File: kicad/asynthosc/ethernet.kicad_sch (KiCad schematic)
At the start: 40 parts, among them J12 RJ45_LED_Shielded, U10 LAN8742A, U11 USBLC6-2P6, U13 USBLC6-2P6, Y2 25MHZ,20PF,30PPM

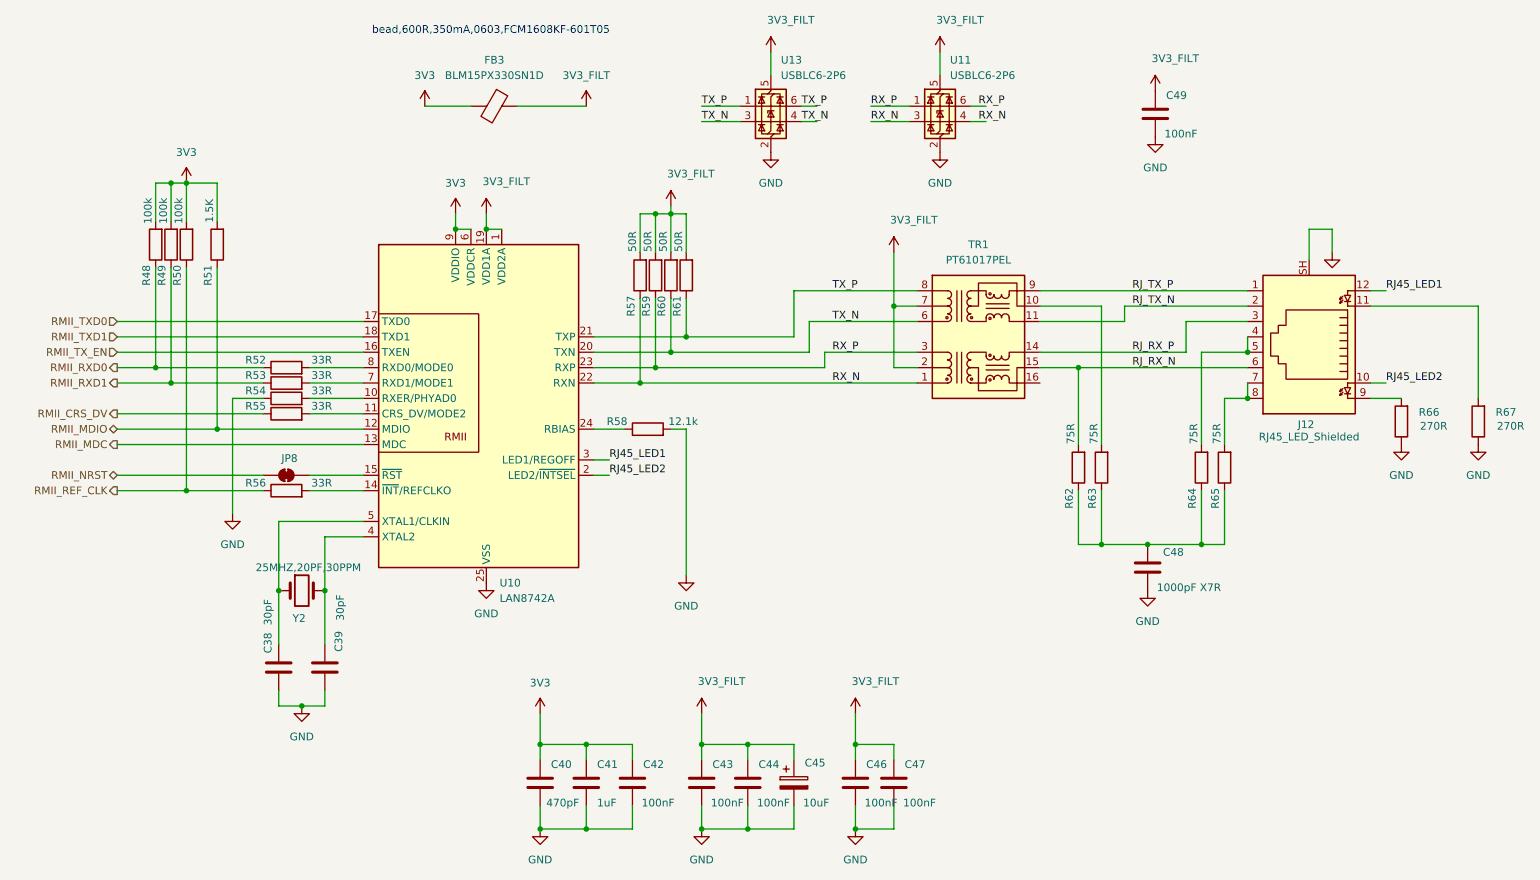
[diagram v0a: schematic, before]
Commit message: sch: pcb: fix pin errors
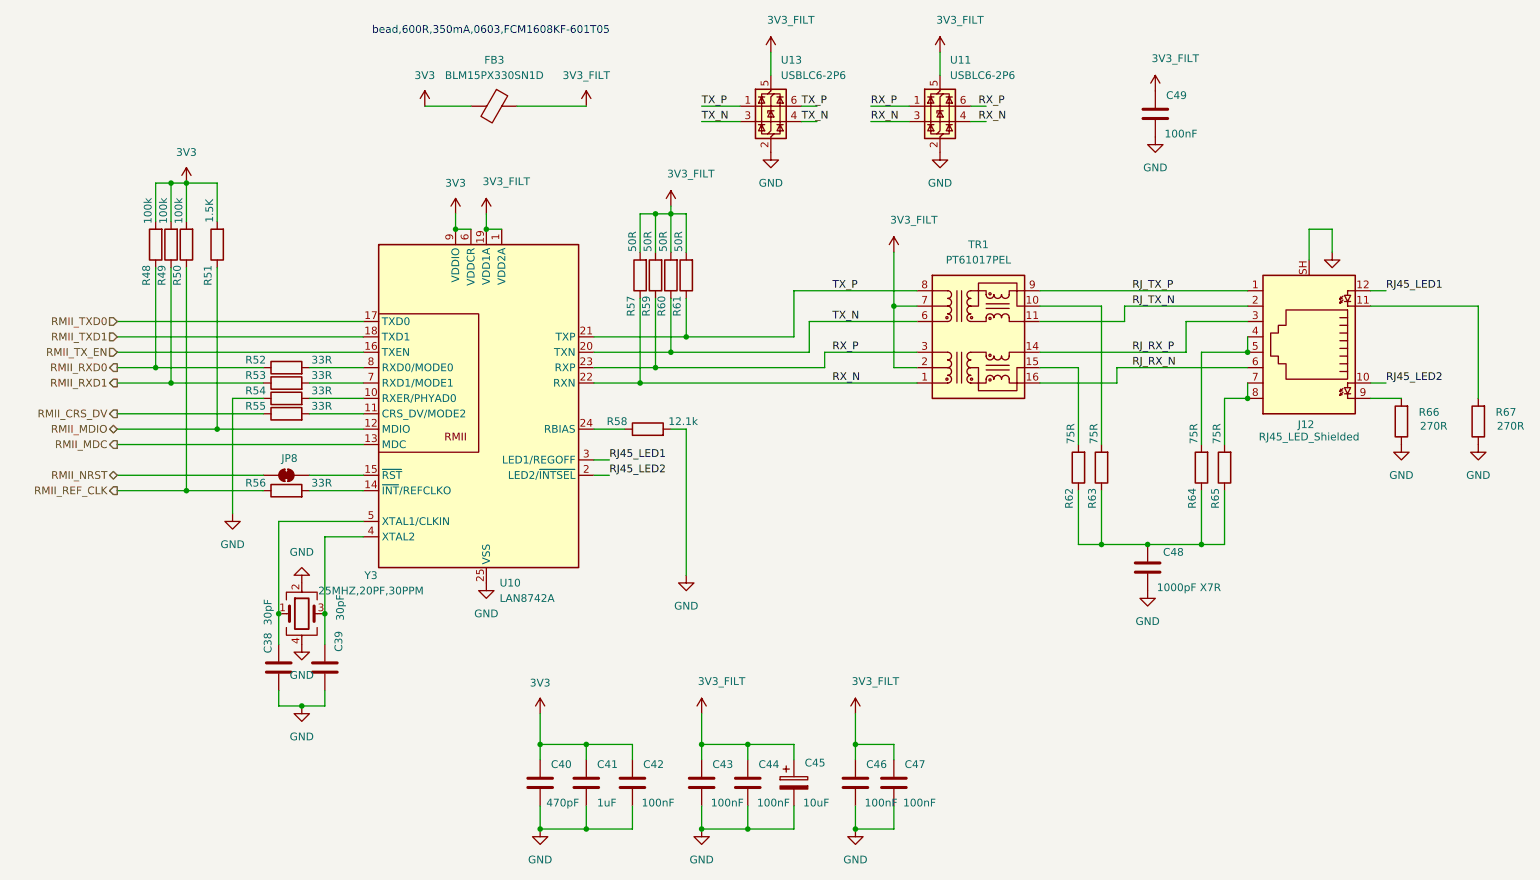
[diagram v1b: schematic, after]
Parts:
- removed Y2: 25MHZ,20PF,30PPM, Crystal:Crystal_SMD_3225-4Pin_3.2x2.5mm, symbol Device:Crystal
- added Y3: 25MHZ,20PF,30PPM, Crystal:Crystal_SMD_3225-4Pin_3.2x2.5mm, symbol Device:Crystal_GND24
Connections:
- net GND: now also Y3.2, Y3.4
- net RJ_RX_N: now also TR1.16 (TX+); no longer R62.2, TR1.15 (C_TX)
- net at C38.2, U10.5 (XTAL1/CLKIN): now also Y3.1
- net at C39.2, U10.4 (XTAL2): now also Y3.3
- new net: R62.2, TR1.15 (C_TX)

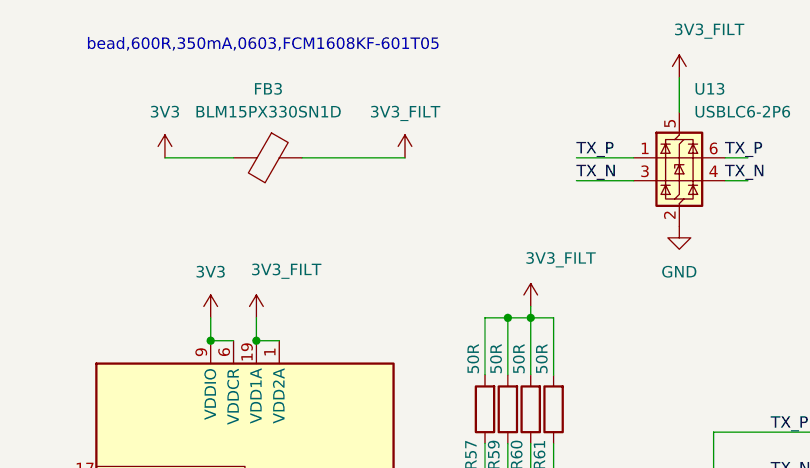
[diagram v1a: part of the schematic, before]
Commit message: pcb: route, add some silkscreen
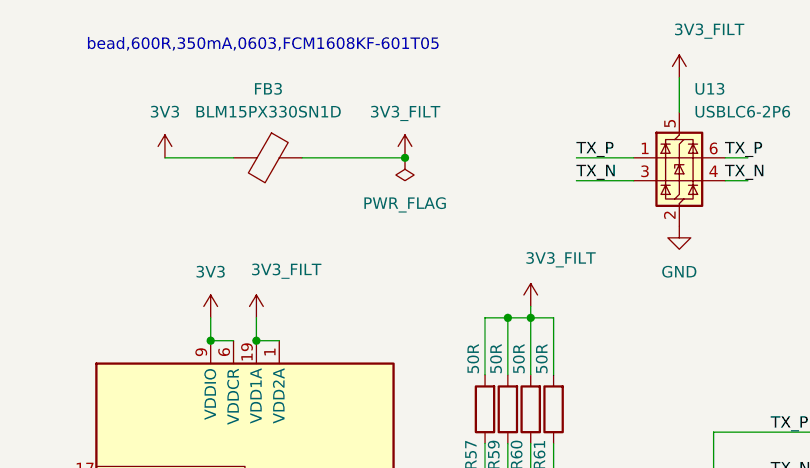
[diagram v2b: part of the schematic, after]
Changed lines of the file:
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@@
 	)
 	(junction
+		(at 106.68 31.75)
+		(diameter 0)
+		(color 0 0 0 0)
+	)
+	(junction
 		(at 118.11 74.93)
 		(diameter 0)
@@
 					(unit 1)
 				)
+			)
+		)
+	)
+	(symbol
+		(lib_id "power:PWR_FLAG")
+		(at 106.68 31.75 180)
+		(unit 1)
+		(exclude_from_sim no)
+		(in_bom yes)
+		(on_board yes)
+		(dnp no)
+		(fields_autoplaced yes)
+		(property "Reference" "#FLG06"
+			(at 106.68 33.655 0)
+			(effects
+				(font
+					(size 1.27 1.27)
+				)
+				(hide yes)
+			)
+		)
+		(property "Value" "PWR_FLAG"
+			(at 106.68 36.83 0)
+			(effects
+				(font
+					(size 1.27 1.27)
+				)
+			)
+		)
+		(property "Footprint" ""
+			(at 106.68 31.75 0)
+			(effects
+				(font
+					(size 1.27 1.27)
+				)
+				(hide yes)
+			)
+		)
+		(property "Datasheet" "~"
+			(at 106.68 31.75 0)
+			(effects
+				(font
+					(size 1.27 1.27)
+				)
+				(hide yes)
+			)
+		)
+		(property "Description" "Special symbol for telling ERC where power comes from"
+			(at 106.68 31.75 0)
+			(effects
+				(font
+					(size 1.27 1.27)
+				)
+				(hide yes)
+			)
+		)
+		(pin "1"
+		)
+		(instances
+			(project "asynthosc"
+				(path "/d73e377a-a016-415f-8824-91cc6e4907b9/dee5e89d-6774-4f8d-b6d8-6a859b9e32e8/354f1097-74a0-4bc1-8721-d2c0e4c9dab3"
+					(reference "#FLG06")
+					(unit 1)
+				)

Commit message: comp: add vertical usb micro-b and rj45 footprints
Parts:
- J12: footprint asynthosc:RJ45_HCTL_HC-RJ45-053-2 -> asynthosc:RJ45_CKMTW_R-RJ45S08P-C000_Vertical; Manufacturer HCTL -> Ckmtw; RefNum HC-RJ45-053-2 -> R-RJ45S08P-C000
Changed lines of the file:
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@@
 			)
 		)
-		(property "Footprint" "asynthosc:RJ45_HCTL_HC-RJ45-053-2"
+		(property "Footprint" "asynthosc:RJ45_CKMTW_R-RJ45S08P-C000_Vertical"
 			(at 226.06 70.485 90)
 			(effects
@@
 			)
 		)
-		(property "Manufacturer" "HCTL"
+		(property "Manufacturer" "Ckmtw"
 			(at 226.06 69.85 0)
 			(effects
@@
 			)
 		)
-		(property "RefNum" "HC-RJ45-053-2 "
+		(property "RefNum" "R-RJ45S08P-C000"
 			(at 226.06 69.85 0)
 			(effects

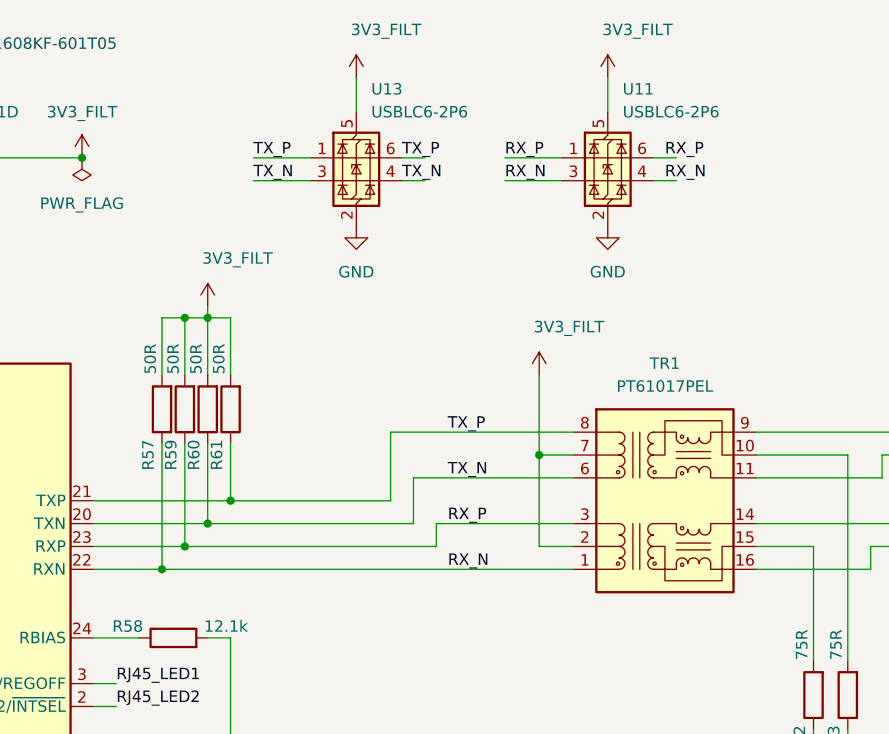
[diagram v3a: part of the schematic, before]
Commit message: pcb: fix some more drc
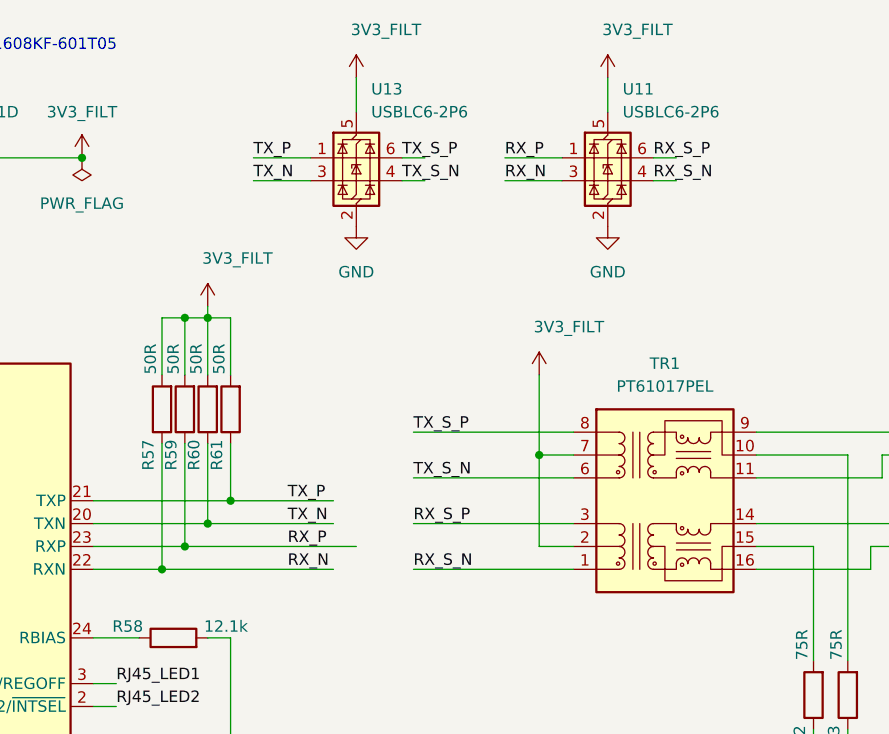
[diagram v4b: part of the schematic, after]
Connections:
- net RX_N: no longer TR1.1 (TD+), U11.4 (I/O2)
- net RX_P: no longer TR1.3 (TD-), U11.6 (I/O1)
- net TX_N: no longer TR1.6 (RD+), U13.4 (I/O2)
- net TX_P: no longer TR1.8 (RD-), U13.6 (I/O1)
- new net RX_S_N: TR1.1 (TD+), U11.4 (I/O2)
- new net RX_S_P: TR1.3 (TD-), U11.6 (I/O1)
- new net TX_S_N: TR1.6 (RD+), U13.4 (I/O2)
- new net TX_S_P: TR1.8 (RD-), U13.6 (I/O1)

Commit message: bom: update mfr, serials and lcsc fields
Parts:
- C45: LCSC (none) -> C72485
- FB3: LCSC (none) -> C160974
- J12: LCSC (none) -> C386764
- TR1: LCSC (none) -> C124001; Manufacturer (none) -> Bourns
- U10: LCSC (none) -> C633284
- U11, U13: LCSC (none) -> C15999
- Y3: LCSC (none) -> C9006
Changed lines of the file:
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@@
 			)
 		)
-		(property "LCSC" ""
+		(property "LCSC" "C15999"
 			(at 165.1 31.75 0)
 			(effects
@@
 			)
 		)
-		(property "LCSC" ""
+		(property "LCSC" "C72485"
 			(at 140.97 143.51 0)
 			(effects
@@
 			)
 		)
+		(property "LCSC" "C9006"
+			(at 59.69 115.57 0)
+			(effects
+				(font
+					(size 1.27 1.27)
+				)
+				(hide yes)
+			)
+		)
 		(pin "2"
 		)
@@
 			)
 		)
-		(property "LCSC" ""
+		(property "LCSC" "C15999"
 			(at 137.16 31.75 0)
 			(effects
@@
 			)
 		)
-		(property "LCSC" ""
+		(property "LCSC" "C124001"
 			(at 171.45 69.85 0)
 			(effects
@@
 			)
 		)
-		(property "Manufacturer" ""
+		(property "Manufacturer" "Bourns"
 			(at 171.45 69.85 0)
 			(effects
@@
 			)
 		)
-		(property "LCSC" ""
+		(property "LCSC" "C633284"
 			(at 90.17 82.55 0)
 			(effects
@@
 			)
 		)
-		(property "LCSC" ""
+		(property "LCSC" "C386764"
 			(at 226.06 69.85 0)
 			(effects
@@
 			)
 		)
-		(property "LCSC" ""
+		(property "LCSC" "C160974"
 			(at 91.44 31.75 0)
 			(effects

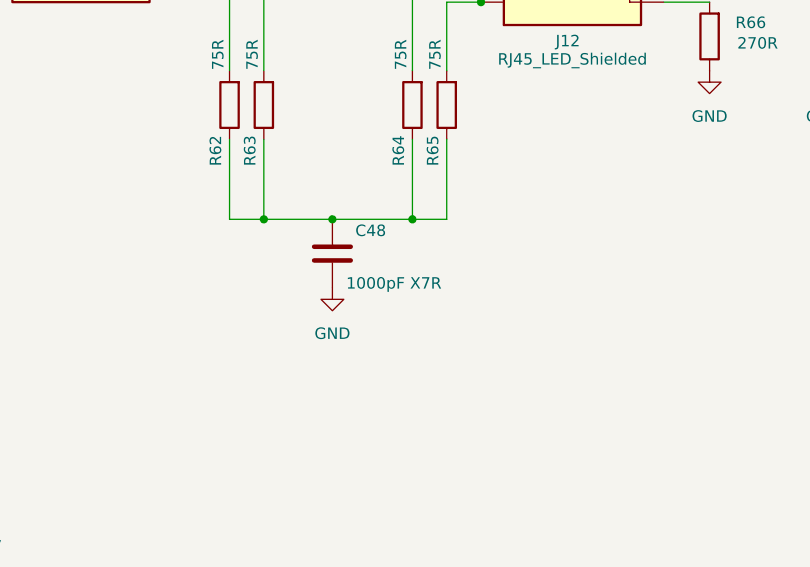
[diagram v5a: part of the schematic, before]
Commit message: bom: update for better bom
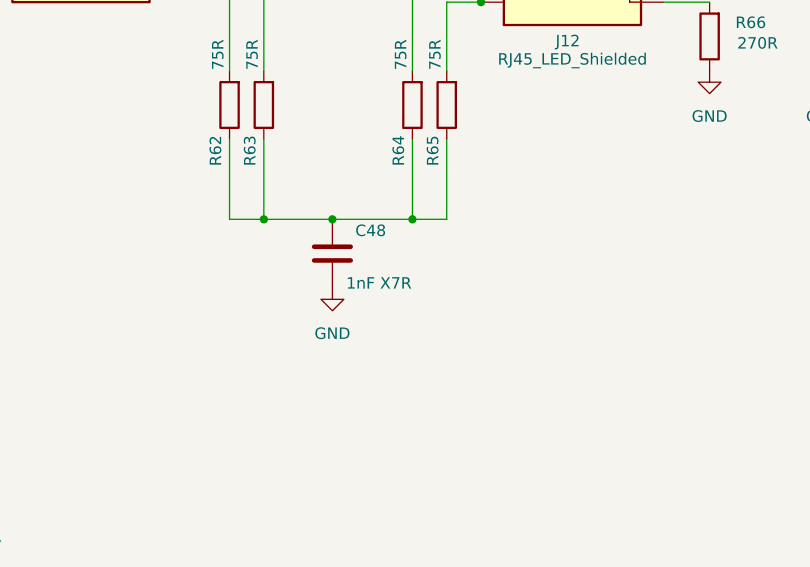
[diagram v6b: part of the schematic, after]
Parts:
- C48: value 1000pF X7R -> 1nF X7R
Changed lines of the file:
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@@
 			)
 		)
-		(property "Value" "1000pF X7R"
+		(property "Value" "1nF X7R"
 			(at 200.914 111.252 0)
 			(effects

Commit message: bom: add jlcpcb field with simplified footprint
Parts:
- C38, C39, C40, C42, C43, C44, C46, C47, C48, C49, R48, R49, R50, R51, R52, R53, R54, R55, R56, R57, R58, R59, R60, R61, R62, R63, R64, R65, R66, R67: JLC (none) -> 0402
- C41: JLC (none) -> 0805
- U10: JLC (none) -> VQFN-24
- U11, U13: JLC (none) -> SOT-666

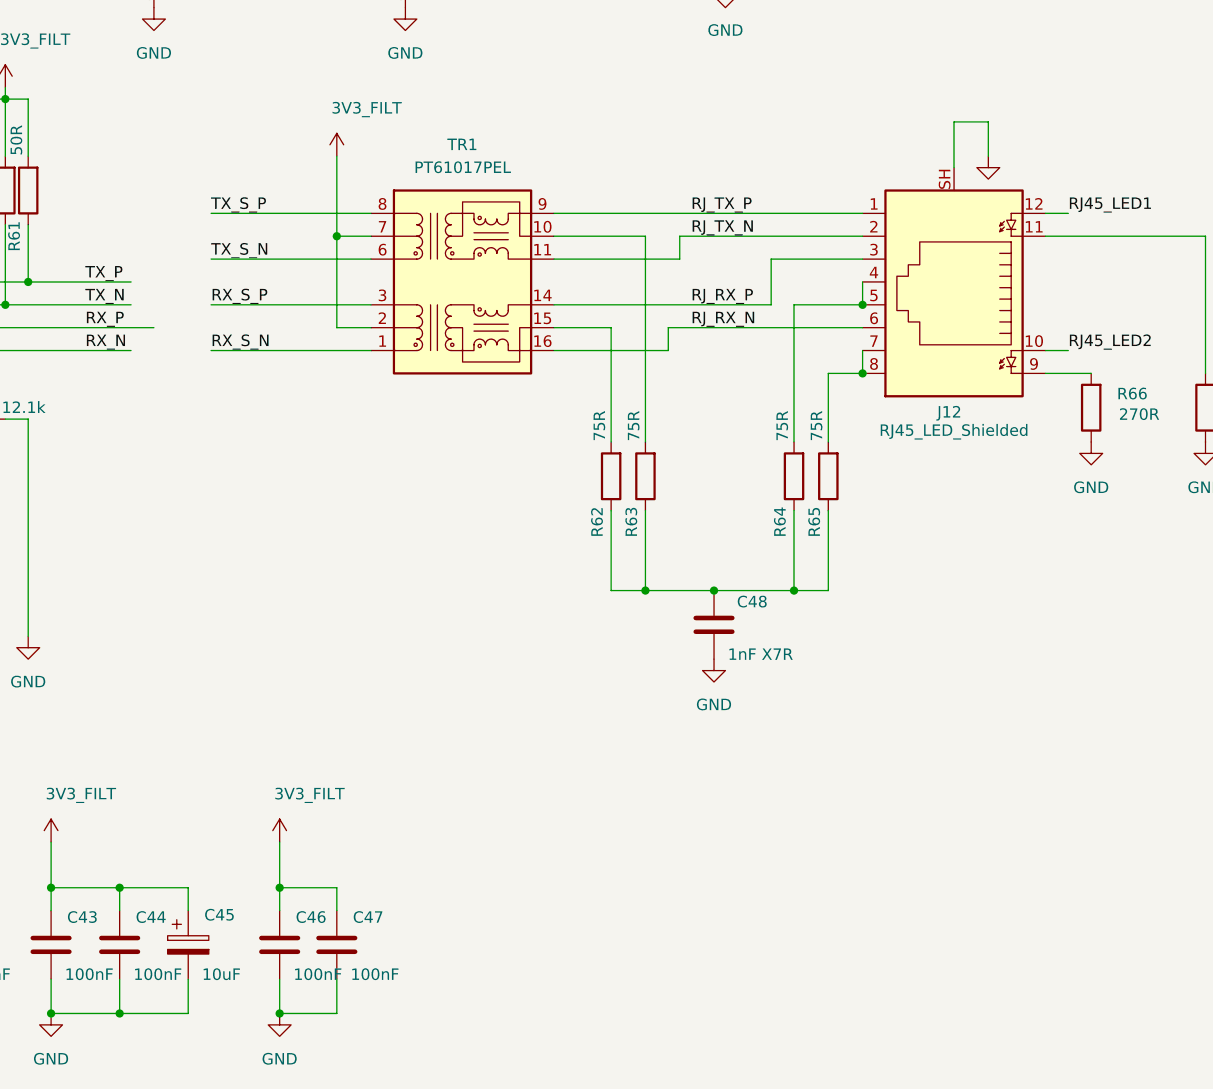
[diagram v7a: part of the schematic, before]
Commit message: bom: dnp for all manually equiped components
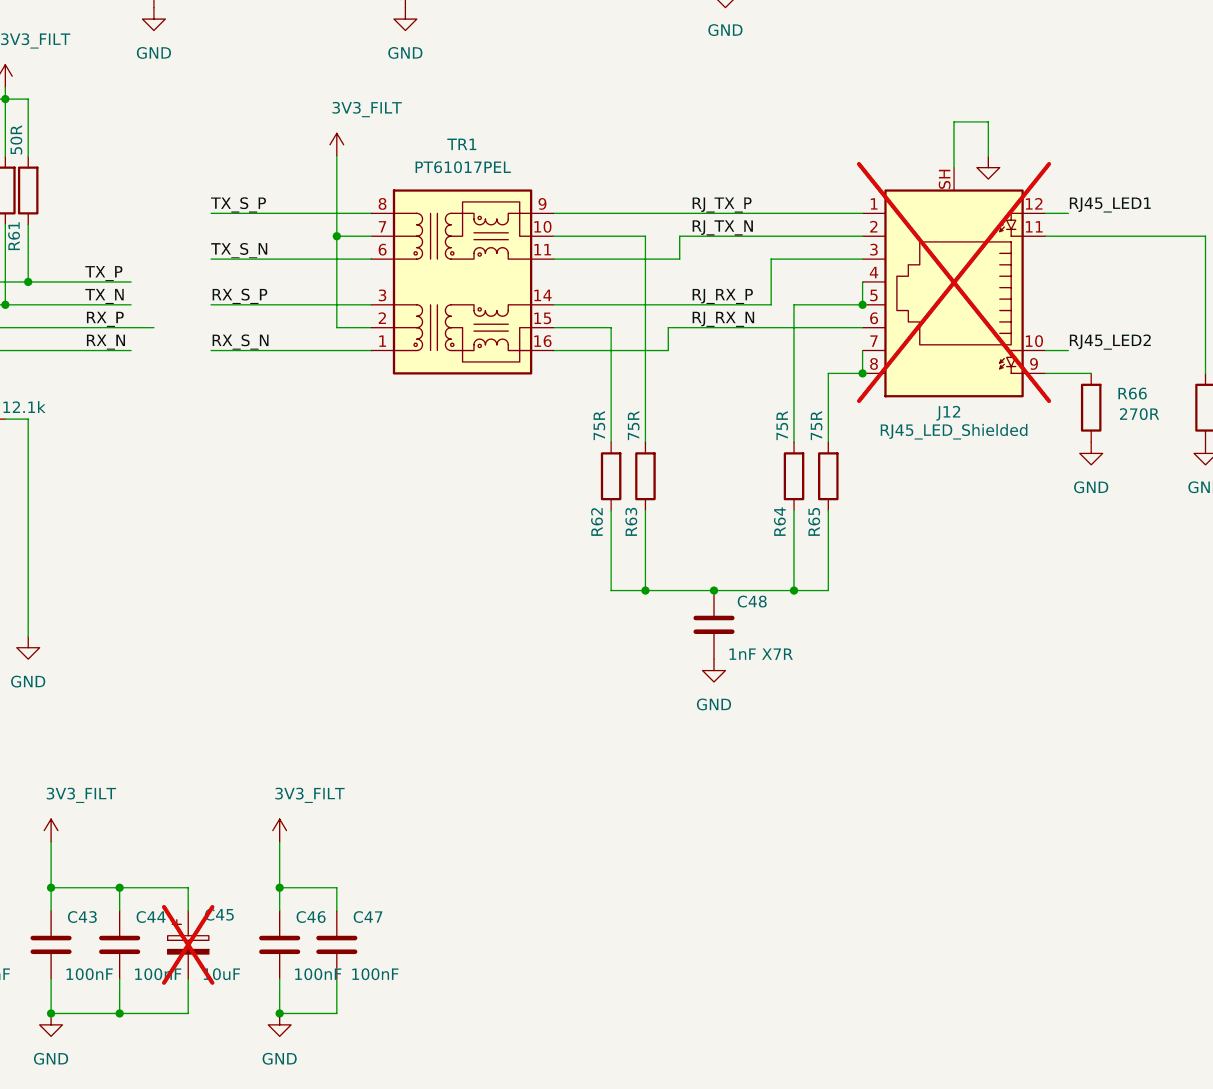
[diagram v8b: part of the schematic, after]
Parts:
- C45, J12: now not fitted
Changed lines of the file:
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@@
 		(in_bom yes)
 		(on_board yes)
-		(dnp no)
+		(dnp yes)
 		(property "Reference" "C45"
 			(at 142.748 140.208 0)
@@
 		(in_bom yes)
 		(on_board yes)
-		(dnp no)
+		(dnp yes)
 		(property "Reference" "J12"
 			(at 225.552 84.328 0)
